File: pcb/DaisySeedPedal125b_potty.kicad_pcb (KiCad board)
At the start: 4 copper layers, 60 x 94 mm, 64 parts, among them J1 Barrel_Jack_Switch, J2 AUDIO_IN_TRS, J3 MIDI IN JACK, J4 AUDIO_OUT_TRS, J6 Conn_01x20_Socket, J7 Conn_01x20_Socket, K1 G6K-2, K2 G6K-2, Q1 SS8050, U1 LD1117S50TR_SOT223, U2 MCP6004, U3 OPA1652AID, U4 H11L1, U5 CPC1018N, U6 CPC1018N, U7 OLED_DISPLAY_SSD1306_SPI

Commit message: Updated kiCad FIles
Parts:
- removed J1: Barrel_Jack_Switch, GuitarPedal125B:Generic_PowerJack
- added GndIN1: ~, TestPoint:TestPoint_THTPad_D2.0mm_Drill1.0mm, F.Cu at (129.8, 44.8)
- added R18: 4.7K, Resistor_SMD:R_0805_2012Metric, F.Cu at (119.9, 62.4)
- added R19: 4.7K, Resistor_SMD:R_0805_2012Metric, F.Cu at (119.9, 65.3)
- added R26: 4.7K, Resistor_SMD:R_0805_2012Metric, F.Cu at (119.9, 68.2)
- added R27: 4.7K, Resistor_SMD:R_0805_2012Metric, F.Cu at (119.9, 71.2)
- added SW2: SW_SPDT, CustomFootprints:ToggleSwitch_THT_SPDT, F.Cu at (124.8, 56.6)
- added VIN1: ~, TestPoint:TestPoint_THTPad_D2.0mm_Drill1.0mm, F.Cu at (135.2, 44.8)
- added potty1: ~, Custom_FP:Potty, B.Cu at (156.4, 75.1)
- added potty2: ~, Custom_FP:Potty, B.Cu at (129.7, 74.9)
- added potty3: ~, Custom_FP:Potty, B.Cu at (156.0, 99.5)
- added potty4: ~, Custom_FP:Potty, B.Cu at (129.4, 99.9)
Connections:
- D1 pad 2: POWER_JACK_PWR -> Net-(D1-A)
- J6 pad 10: unconnected-(J6-Pin_10-Pad10) -> UPDI1
- J6 pad 13: unconnected-(J6-Pin_13-Pad13) -> OLED_DISPLAY_SPI_RESET
- J6 pad 14: POT_6 -> ENABLE_AUDIO_MUTE
- J6 pad 15: POT_5 -> unconnected-(J6-Pin_15-Pad15)
- J6 pad 16: POT_4 -> unconnected-(J6-Pin_16-Pad16)
- J6 pad 17: POT_3 -> unconnected-(J6-Pin_17-Pad17)
- J6 pad 18: POT_2 -> unconnected-(J6-Pin_18-Pad18)
- J6 pad 19: POT_1 -> unconnected-(J6-Pin_19-Pad19)
- J6 pad 5: Net-(J6-Pin_5) -> unconnected-(J6-Pin_5-Pad5)
- J6 pad 7: unconnected-(J6-Pin_7-Pad7) -> UPDI4
- J6 pad 8: unconnected-(J6-Pin_8-Pad8) -> UPDI3
- J6 pad 9: unconnected-(J6-Pin_9-Pad9) -> UPDI2
- J7 pad 16: ENCODER_1_CLICK -> unconnected-(J7-Pin_16-Pad16)
- J7 pad 17: ENCODER_1_B -> unconnected-(J7-Pin_17-Pad17)
- J7 pad 18: ENCODER_1_A -> unconnected-(J7-Pin_18-Pad18)
- J7 pad 6: unconnected-(J7-Pin_6-Pad6) -> SW1_LEFT
- J7 pad 7: unconnected-(J7-Pin_7-Pad7) -> SW1_RIGHT
- J7 pad 8: ENABLE_AUDIO_MUTE -> I2C_SDA
- J7 pad 9: OLED_DISPLAY_SPI_RESET -> I2C_SCL
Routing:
- net (no net): track 115.4 -> 0.00 mm, vias 2 -> 0
- net +3.3VA: track 81.6 -> 0.00 mm
- net AUDIO_OUT_JACK_LEFT: track 62.0 -> 0.00 mm, vias 2 -> 0
- net AUDIO_OUT_JACK_RIGHT: track 57.1 -> 0.00 mm, vias 2 -> 0
- net ENCODER_1_CLICK: track 54.1 -> 0.00 mm
- net Net-(J6-Pin_5): track 43.9 -> 0.00 mm
- net POT_3: track 38.4 -> 0.00 mm
- net GND: track 49.5 -> 11.6 mm, vias 38 -> 0
- net AUDIO_IN_JACK_RIGHT: track 34.4 -> 0.00 mm, vias 1 -> 0
- net POT_6: track 26.8 -> 0.00 mm
- net ENABLE_AUDIO_MUTE: track 26.4 -> 3.18 mm, vias 1 -> 0
- net POT_2: track 20.4 -> 0.00 mm
- net POT_1: track 19.7 -> 0.00 mm
- net POT_4: track 12.8 -> 0.00 mm
- net POT_5: track 9.29 -> 0.00 mm
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- added copper zone on In1.Cu, net AUDIO_IN_JACK_LEFT
- added copper zone on In2.Cu, net AUDIO_IN_JACK_LEFT
- removed copper zone on In1.Cu, net GND
- removed copper zone on In2.Cu, net GND

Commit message: Lots of updates to Schematic and pcb design
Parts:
- added C18: 100nF, Capacitor_SMD:C_0805_2012Metric, F.Cu at (160.5, 61.8)
- added C19: 10uF, Capacitor_SMD:C_0805_2012Metric, F.Cu at (160.5, 59.6)
- added C20: 10uF, Capacitor_SMD:C_0805_2012Metric, F.Cu at (124.7, 61.9)
- added C21: 100nF, Capacitor_SMD:C_0805_2012Metric, F.Cu at (124.7, 59.8)
- added C22: 10uF, Capacitor_SMD:C_0805_2012Metric, F.Cu at (117.3, 84.2)
- added C23: 100nF, Capacitor_SMD:C_0805_2012Metric, F.Cu at (119.4, 84.2)
- added C24: 10uF, Capacitor_SMD:C_0805_2012Metric, F.Cu at (151.8, 85.0)
- added C25: 100nF, Capacitor_SMD:C_0805_2012Metric, F.Cu at (153.9, 85.0)
- added C26: 10UF, Capacitor_SMD:C_0805_2012Metric, F.Cu at (144.9, 49.7)
- added C27: 100NF, Capacitor_SMD:C_0805_2012Metric, F.Cu at (151.3, 57.4)
- added C28: 100NF, Capacitor_SMD:C_0805_2012Metric, F.Cu at (144.9, 47.5)
- added C29: 100NF, Capacitor_SMD:C_0805_2012Metric, F.Cu at (162.4, 42.7)
- added C30: 10UF, Capacitor_SMD:C_0805_2012Metric, F.Cu at (149.2, 57.4)
- added R28: 4.7K, Resistor_SMD:R_0805_2012Metric, F.Cu at (142.2, 76.4)
- added R29: 4.7K, Resistor_SMD:R_0805_2012Metric, F.Cu at (144.8, 76.4)
- added REF**: Enclosure_FP, Custom_FP:Enclosure_FP, F.Cu at (142.4, 100.0)
- added U8: LM7805_TO220, Package_TO_SOT_THT:TO-220-3_Vertical, F.Cu at (144.1, 53.9)
- SW2: moved to B.Cu
- potty1, potty2, potty3, potty4: value ~ -> Custom_Encoder/LED_Module
- moved R24 48.6 mm to (122.2, 121.7)
- moved R25 47.6 mm to (159.1, 121.9)
- moved SW2 22.8 mm to (142.0, 71.5)
- moved potty2 19.3 mm to (124.0, 56.5), turned to 0 degrees
- moved R15 19.1 mm to (148.1, 100.4), turned to 90 degrees
- moved R18 19.0 mm to (138.1, 67.9)
- moved potty1 18.9 mm to (160.0, 56.5), turned to 0 degrees
- moved D2 17.4 mm to (138.0, 47.9), turned to 180 degrees
- moved potty4 16.8 mm to (124.0, 84.0), turned to -90 degrees
- moved potty3 16.0 mm to (160.0, 84.0), turned to -90 degrees
- moved R13 15.5 mm to (150.2, 104.2)
- moved C15 15.5 mm to (148.0, 104.2)
- moved R19 15.0 mm to (134.5, 68.6), turned to -90 degrees
- moved C4 13.3 mm to (162.4, 45.0), turned to 0 degrees
- moved R17 13.2 mm to (129.1, 46.2), turned to 0 degrees
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- renumbered VIN1 to 9V, GndIN1 to GND
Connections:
- C13 pad 1: +5V -> +5VA
- C14 pad 1: +5V -> +5VA
- C4 pad 1: +5V -> +5VA
- C5 pad 1: +5V -> +5VA
- C6 pad 1: +5V -> +5VA
- D3 pad 1: +5V -> +5VA
- D4 pad 1: +5V -> +5VA
- K1 pad 1: +5V -> +5VA
- K2 pad 1: +5V -> +5VA
- R11 pad 1: +5V -> +5VA
- R18 pad 1: +5V -> UPDI1
- R18 pad 2: UPDI1 -> +5V
- R19 pad 1: +5V -> UPDI2
- R19 pad 2: UPDI2 -> +5V
- R26 pad 1: +5V -> UPDI3
- R26 pad 2: UPDI3 -> +5V
- R27 pad 1: +5V -> UPDI4
- R27 pad 2: UPDI4 -> +5V
- R3 pad 1: +5V -> +5VA
- R9 pad 1: +5V -> +5VA
- U1 pad 2: +5V -> +5VA
- U2 pad 4: +5V -> +5VA
- U3 pad 8: +5V -> +5VA
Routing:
- net Net-(LED1-A): track 124.9 -> 2.36 mm, vias 1 -> 0
- net Net-(LED2-A): track 80.1 -> 2.27 mm, vias 1 -> 0
- net LED_2: track 3.52 -> 77.5 mm, vias 0 -> 1
- net +5V: track 73.7 -> 0.00 mm, vias 2 -> 0
- net I2C_SDA: track 0.00 -> 67.3 mm
- net LED_1: track 3.52 -> 69.4 mm, vias 0 -> 1
- net AUDIO_OUT_JACK_LEFT: track 0.00 -> 56.1 mm
- net AUDIO_OUT_JACK_RIGHT: track 0.00 -> 48.5 mm
- net OLED_DISPLAY_SPI_RESET: track 0.00 -> 34.4 mm
- net UPDI4: track 0.00 -> 28.2 mm
- net AUDIO_IN_JACK_RIGHT: track 0.00 -> 27.7 mm
- net +5VA: track 0.00 -> 18.9 mm
- net BYPASS_LEFT_RETURN: track 18.8 -> 1.97 mm, vias 2 -> 0
- net I2C_SCL: track 0.00 -> 16.3 mm
- net DISABLE_AUDIO_BYPASS: track 5.10 -> 20.5 mm
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- added copper zone on F.Cu, net +5VA
- removed copper zone on F.Cu, net +3.3V
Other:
- board text added: "Potty Guitar Pedal Made by Jeremy Cooper 02/2026"
- board text removed: "Daisy Seed Guitar Pedal 125B (Rev 6) Made by Keith Shepherd 2/25/2024"
- board text removed: "J4"
- board text removed: "J5"
- board text removed: "Midi Out"
- board text removed: "Power In"

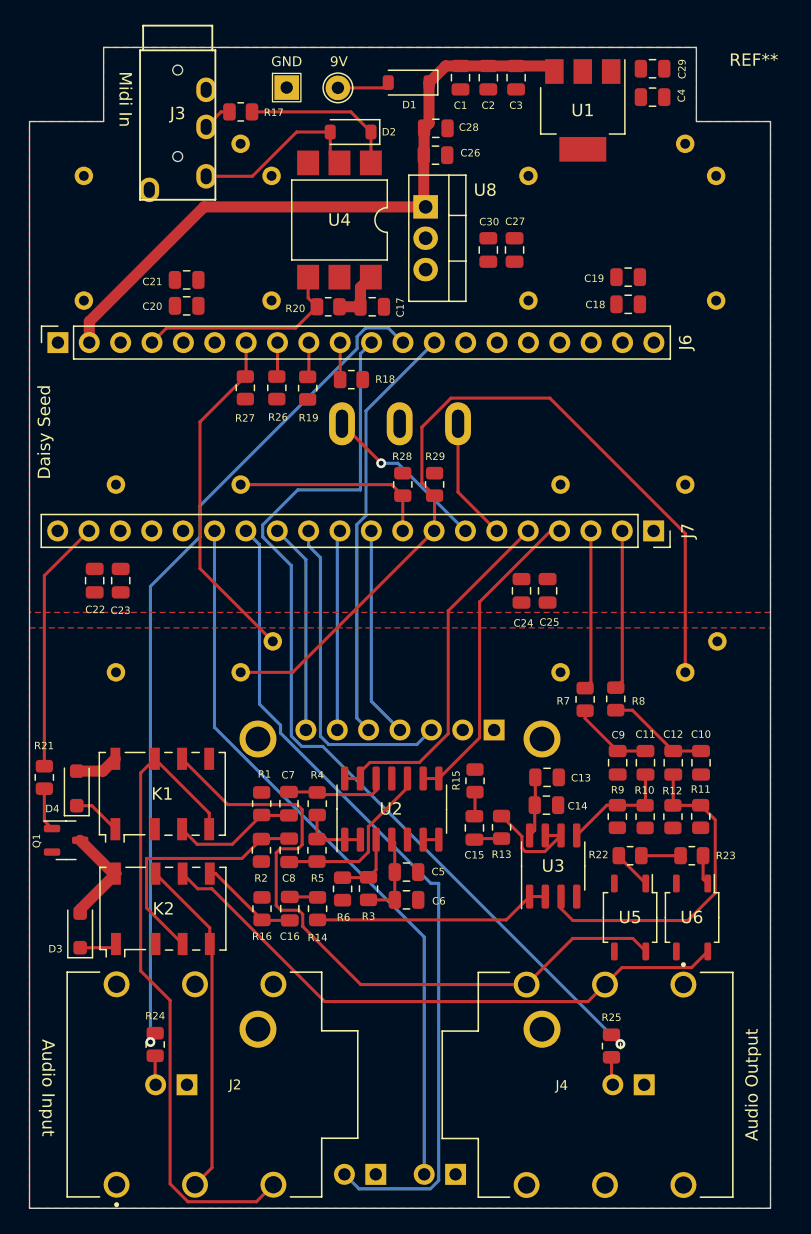
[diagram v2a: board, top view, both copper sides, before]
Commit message: Updated PCB, started laying tracks.
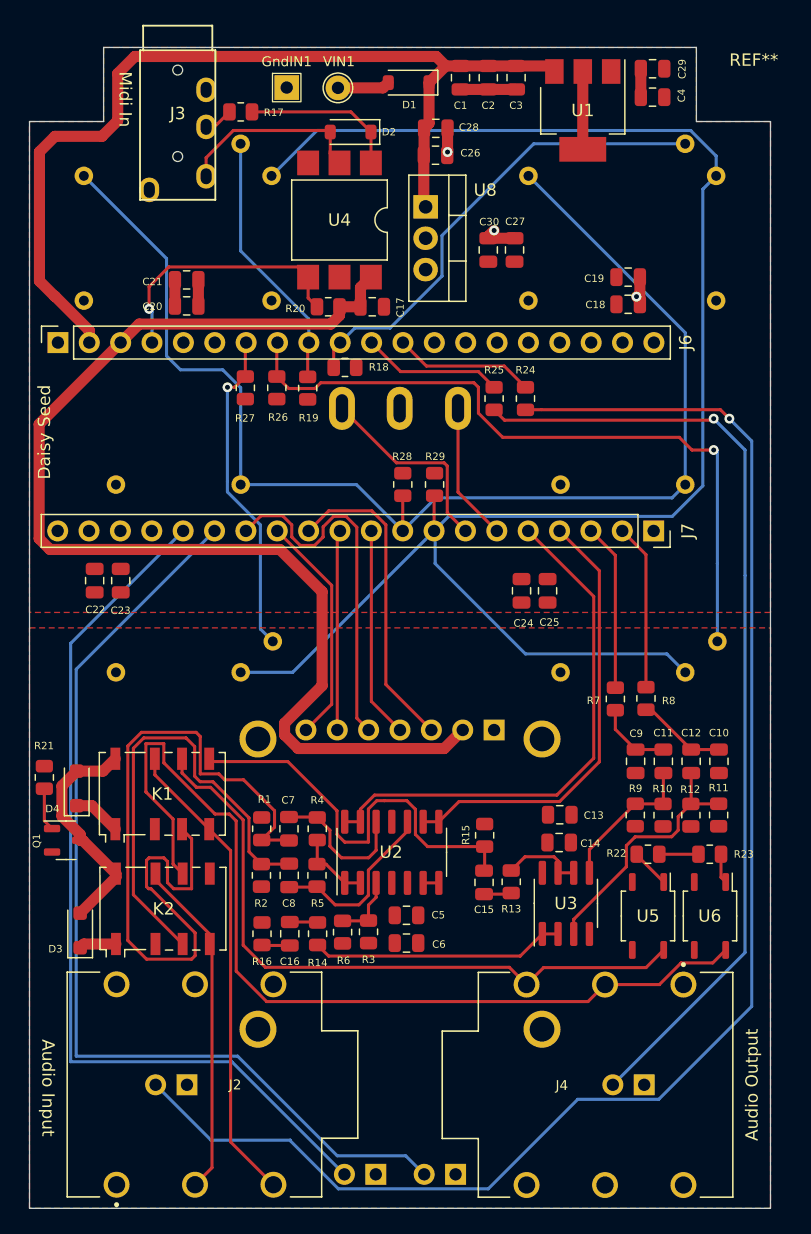
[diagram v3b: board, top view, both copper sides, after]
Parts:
- moved R24 60.3 mm to (152.2, 69.4)
- moved R25 53.3 mm to (149.6, 69.4)
- moved C15 4.48 mm to (148.8, 108.6)
- moved R13 4.48 mm to (151.0, 108.6)
- moved R15 4.48 mm to (148.9, 104.8)
- moved C5 3.50 mm to (142.5, 111.3)
- moved C6 3.50 mm to (142.5, 113.5)
- moved R3 3.50 mm to (139.4, 112.6)
- moved R6 3.50 mm to (137.3, 112.6)
- moved U2 3.50 mm to (141.3, 106.2)
- moved C13 3.20 mm to (154.9, 103.1)
- moved C14 3.20 mm to (154.9, 105.4)
- moved U3 3.20 mm to (155.4, 110.3)
- moved R7 2.45 mm to (159.4, 93.8)
- moved R8 2.45 mm to (161.9, 93.7)
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- renumbered GND to GndIN1, 9V to VIN1
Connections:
- J6 pad 13: OLED_DISPLAY_SPI_RESET -> unconnected-(J6-Pin_13-Pad13)
- J7 pad 14: FOOT_SWITCH_1 -> OLED_DISPLAY_SPI_RESET
- J7 pad 16: unconnected-(J7-Pin_16-Pad16) -> FOOT_SWITCH_1
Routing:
- net Net-(LED1-A): track 2.36 -> 123.1 mm, vias 0 -> 1
- net +3.3V: track 4.45 -> 95.4 mm
- net I2C_SCL: track 16.3 -> 104.5 mm
- net Net-(LED2-A): track 2.27 -> 77.6 mm, vias 0 -> 1
- net I2C_SDA: track 67.3 -> 138.7 mm
- net LED_2: track 77.5 -> 11.4 mm, vias 1 -> 0
- net LED_1: track 69.4 -> 11.4 mm, vias 1 -> 0
- net UPDI3: track 2.77 -> 58.0 mm, vias 0 -> 1
- net BYPASS_LEFT_SEND: track 10.2 -> 64.1 mm
- net UPDI1: track 3.00 -> 38.8 mm
- net BYPASS_LEFT_RETURN: track 1.97 -> 33.9 mm
- net AUDIO_OUT_JACK_RIGHT: track 48.5 -> 77.1 mm
- net +9V: track 54.0 -> 77.0 mm
- net DISABLE_AUDIO_BYPASS: track 20.5 -> 0.00 mm
- net FOOT_SWITCH_2: track 59.1 -> 79.3 mm
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- added copper zone on In1.Cu, net GND
- added copper zone on In2.Cu, net GND
- removed copper zone on In1.Cu, net AUDIO_IN_JACK_LEFT
- removed copper zone on In2.Cu, net AUDIO_IN_JACK_LEFT

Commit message: Updated pcb and 3D models
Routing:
- net ENABLE_AUDIO_MUTE: track 3.18 -> 67.0 mm
- net +5VA: track 15.5 -> 76.3 mm
- net GND: track 14.7 -> 42.9 mm, vias 3 -> 25
- net DISABLE_AUDIO_BYPASS: track 0.00 -> 20.6 mm, vias 0 -> 1
- net BYPASS_RIGHT_RETURN: track 2.27 -> 11.0 mm, vias 0 -> 2

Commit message: Updated pcb design
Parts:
- moved C13 0.29 mm to (154.9, 103.4)
- moved R9 0.23 mm to (161.0, 102.9)
- moved C14 0.15 mm to (155.0, 105.5)
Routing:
- net +5VA: track 76.3 -> 92.6 mm, vias 0 -> 6
- net I2C_SDA: track 138.7 -> 149.2 mm, vias 0 -> 1
- net +3.3V: track 95.4 -> 88.7 mm, vias 0 -> 2
- net GND: track 42.9 -> 46.6 mm, vias 25 -> 27
- net Net-(U3B-+): track 11.9 -> 14.9 mm
- net OLED_DISPLAY_SPI_CS: track 18.8 -> 17.1 mm
- net UPDI4: track 26.7 -> 25.2 mm
- net ENABLE_AUDIO_MUTE: track 67.0 -> 66.1 mm
- net DISABLE_AUDIO_BYPASS: vias 1 -> 0

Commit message: Updates
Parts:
- removed SW2: SW_SPDT, CustomFootprints:ToggleSwitch_THT_SPDT
- moved C29 71.3 mm to (168.3, 113.7)
- moved C4 68.7 mm to (164.6, 113.7), turned to 180 degrees
- moved U1 63.7 mm to (167.1, 109.0), turned to 180 degrees
- moved C3 63.2 mm to (169.4, 104.0), turned to 180 degrees
- moved U6 7.44 mm to (159.7, 111.1)
- moved U5 7.44 mm to (154.6, 111.1)
- moved R23 7.15 mm to (159.9, 106.2)
- moved U3 6.54 mm to (148.9, 110.9)
- moved R22 5.82 mm to (156.3, 106.2)
- moved C27 3.89 mm to (155.1, 57.0)
- moved C30 3.89 mm to (153.0, 57.0)
- moved C15 3.89 mm to (147.1, 105.1)
- moved R13 3.86 mm to (149.3, 105.1)
- moved U8 3.74 mm to (147.8, 53.7)
- moved C14 3.00 mm to (152.2, 104.4)
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- renumbered GndIN1 to GND, VIN1 to Vin
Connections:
- J7 pad 6: SW1_LEFT -> unconnected-(J7-Pin_6-Pad6)
- J7 pad 7: SW1_RIGHT -> unconnected-(J7-Pin_7-Pad7)
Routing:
- net +9V: track 77.0 -> 148.6 mm
- net +5V: track 2.10 -> 46.3 mm, vias 0 -> 7
- net GND: track 46.6 -> 86.7 mm, vias 27 -> 41
- net +5VA: track 92.6 -> 71.2 mm, vias 6 -> 7
- net SW1_RIGHT: track 16.3 -> 0.00 mm
- net SW1_LEFT: track 11.2 -> 0.00 mm
- net ENABLE_AUDIO_MUTE: track 66.1 -> 74.5 mm
- net AUDIO_OUT_JACK_LEFT: track 54.3 -> 47.0 mm
- net AUDIO_OUT_JACK_RIGHT: track 77.1 -> 70.2 mm
- net Net-(U3A--): track 20.6 -> 13.8 mm
- net Net-(U3A-+): track 21.0 -> 26.3 mm
- net Net-(U3B-+): track 14.9 -> 19.1 mm
- net UPDI1: track 38.8 -> 41.7 mm
- net I2C_SCL: track 104.5 -> 102.5 mm
- net UPDI4: track 25.2 -> 26.1 mm
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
